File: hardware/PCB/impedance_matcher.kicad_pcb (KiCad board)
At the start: 4 copper layers, 72 x 63 mm, 48 parts, among them Q1 PC817, U1 TLV2372IP

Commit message: Hackerfab Logo
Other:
- board text added: "at CMU"

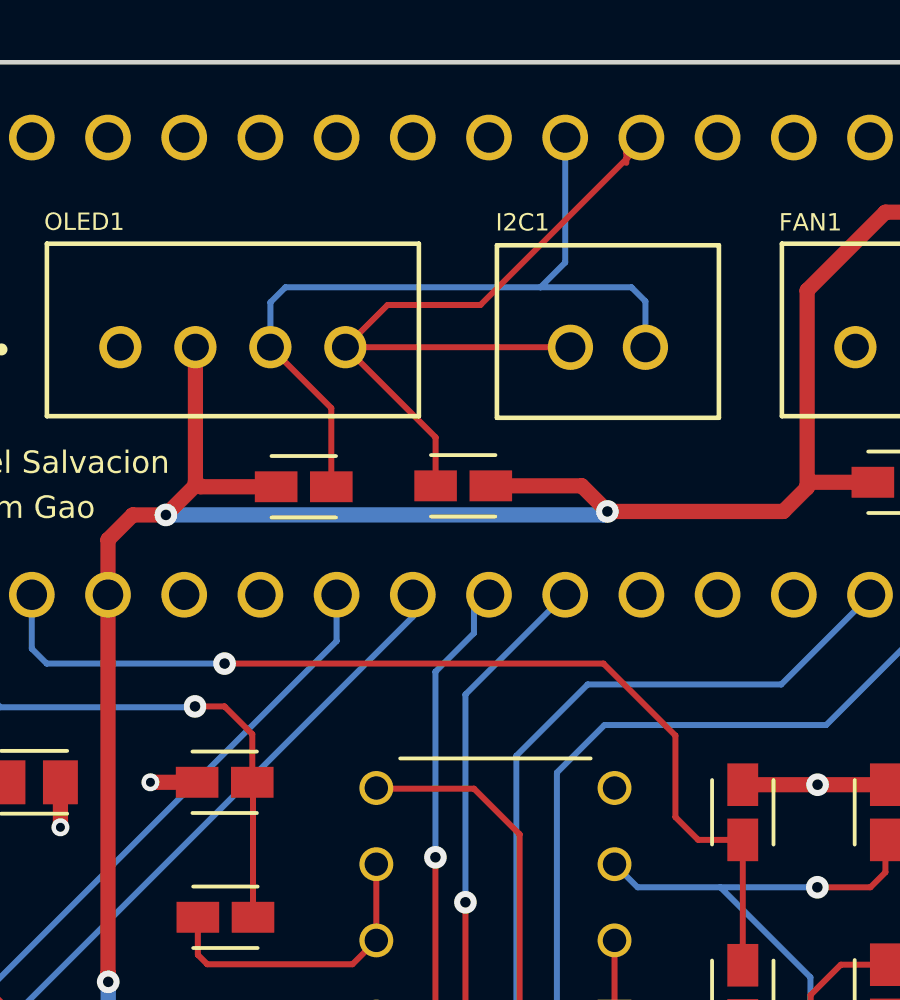
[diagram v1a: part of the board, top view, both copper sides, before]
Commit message: Clean up nets and layers
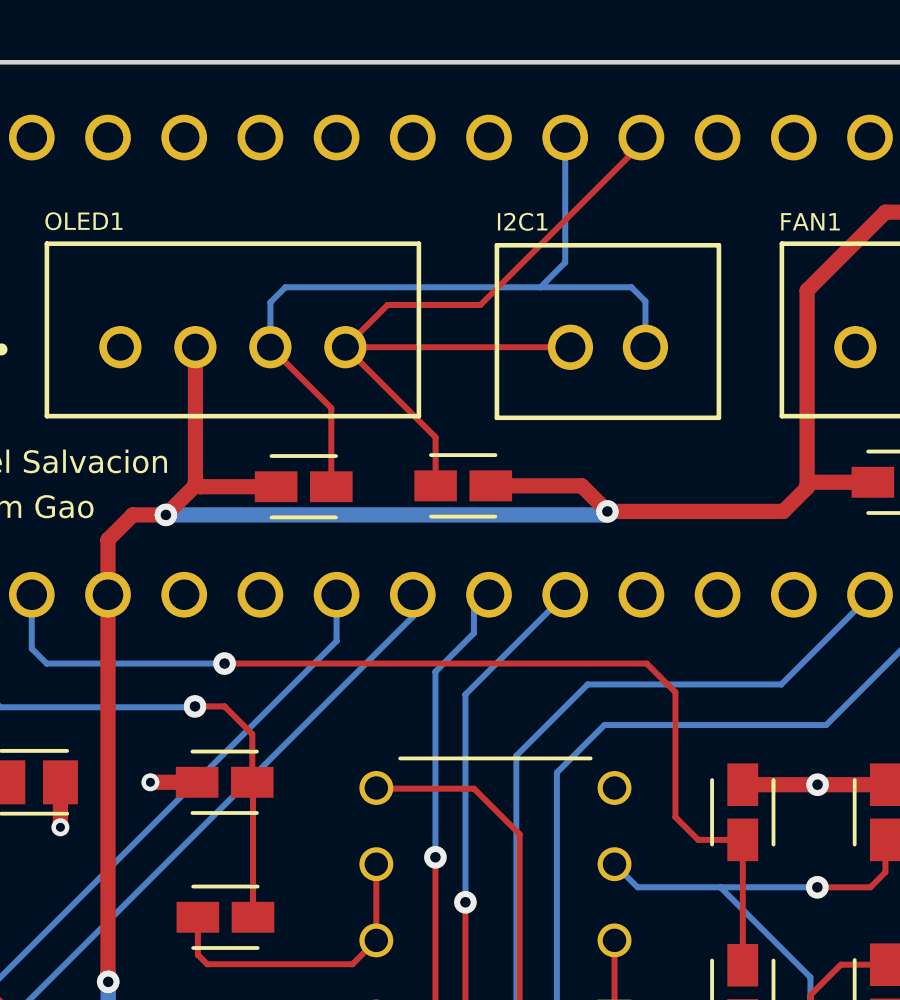
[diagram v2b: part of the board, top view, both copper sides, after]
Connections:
- net Net-(CR1-Pad1) renamed /NET_REVPOL
- net Net-(D1-A) renamed /SW_NODE
- net Net-(DRIVER1-VM) renamed /VM_DRV1
- net Net-(DRIVER2-VM) renamed /VM_DRV2
- net Net-(FAN1-Pin_3) renamed /FAN_CTRL
- net Net-(FB1-Pad2) renamed /FB1_OUT
- net Net-(POWER1-Pin_2) renamed /VIN
- net Net-(STEP_UP0-FB) renamed /FB_DIV
- net Net-(TRANSMIT1-Pin_1) renamed /TX_DRAIN
- net Net-(TRANSMIT1-Pin_2) renamed /TX_GATE
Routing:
- net /FWD_OUT: track 33.6 -> 34.4 mm

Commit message: SWR input protection
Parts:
- added D2: BAV99S, Package_TO_SOT_SMD:SOT-363_SC-70-6, F.Cu at (93.0, 50.5)
- added R14: 1k, Resistor:RESC2012X65, F.Cu at (94.5, 47.5)
- added R15: 1k, Resistor:RESC2012X65, F.Cu at (94.5, 53.5)
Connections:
- U1 pad 3: /FWD_IN -> /FWD_BUF
- U1 pad 5: /REV_IN -> /REV_BUF
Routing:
- net /REV_BUF: track 0.00 -> 33.2 mm
- net /REV_IN: track 43.6 -> 20.2 mm
- net 12V: track 20.8 -> 41.7 mm, vias 0 -> 3
- net /FWD_BUF: track 0.00 -> 14.0 mm, vias 0 -> 1
- net /FWD_IN: track 31.2 -> 25.3 mm, vias 1 -> 0
- net GND: track 22.3 -> 24.9 mm, vias 11 -> 13

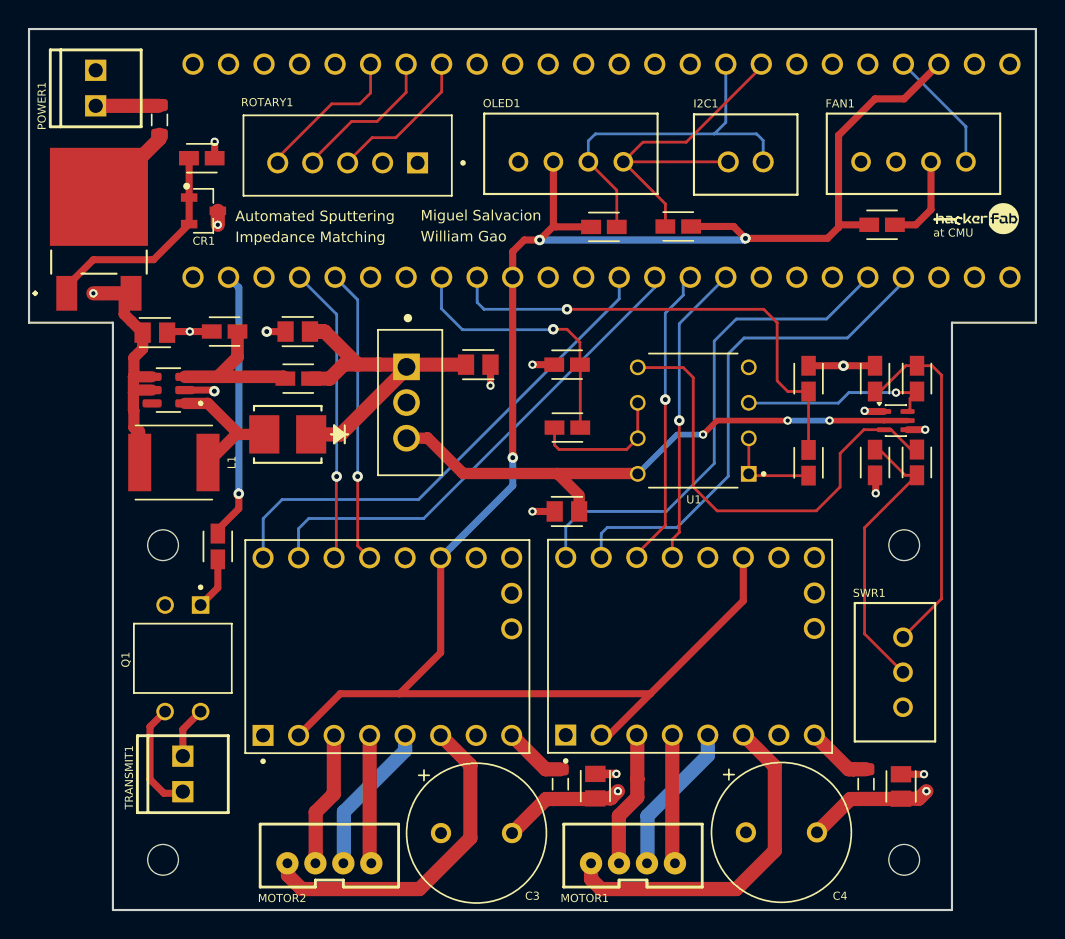
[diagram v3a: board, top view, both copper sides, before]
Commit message: change i2c1, rotary1, oled1, fan1, swr1 to JST PH 2.0mm and update C3/C4 pad1 to be 5V instead of pad2
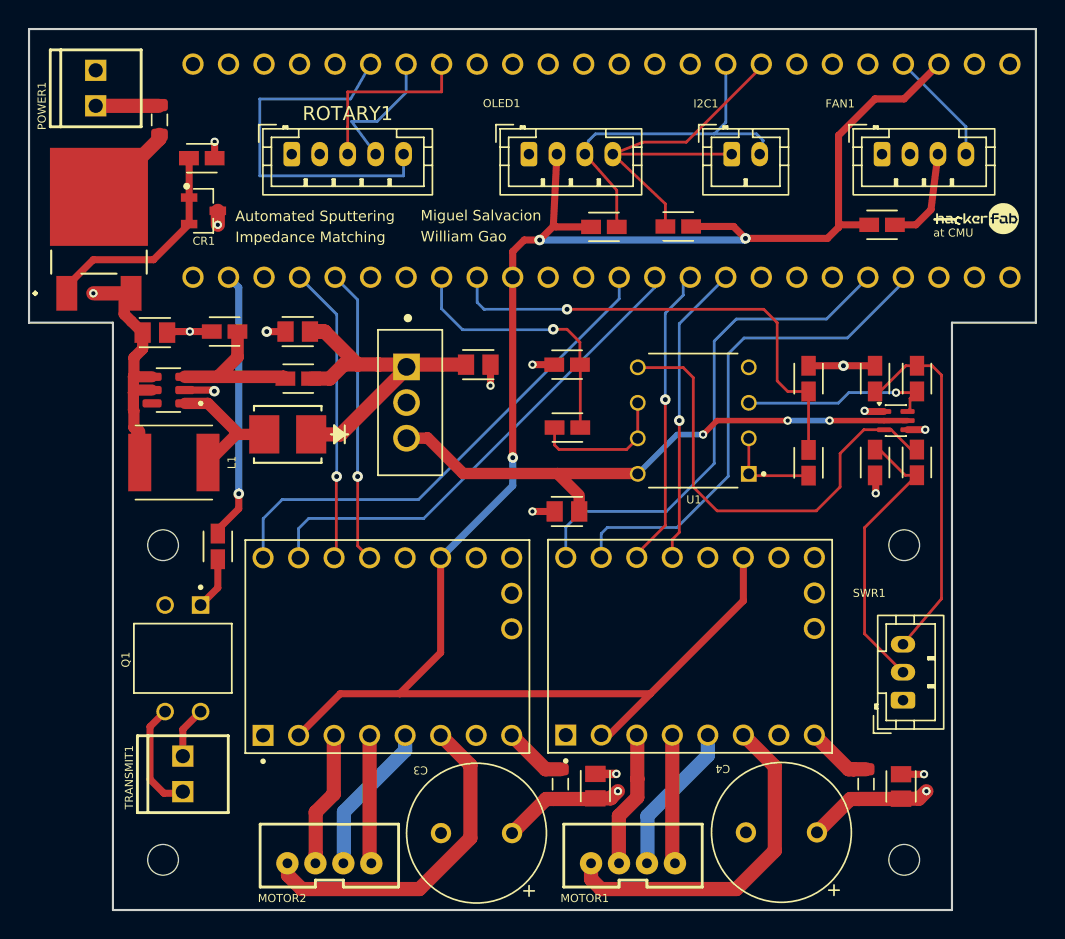
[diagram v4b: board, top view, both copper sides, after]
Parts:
- FAN1, OLED1: footprint Project Connectors:B4B-XH-A -> Connector_JST:JST_PH_B4B-PH-K_1x04_P2.00mm_Vertical
- I2C1: footprint Project Connectors:B2B-XH-A -> Connector_JST:JST_PH_B2B-PH-K_1x02_P2.00mm_Vertical
- ROTARY1: footprint B5B-XH-A:JST_B5B-XH-A -> Connector_JST:JST_PH_B5B-PH-K_1x05_P2.00mm_Vertical
- SWR1: footprint Project Connectors:B3B-XH-A -> Connector_JST:JST_PH_B3B-PH-K_1x03_P2.00mm_Vertical
- moved ROTARY1 4.00 mm to (49.8, 31.4)
- moved I2C1 2.32 mm to (81.2, 31.4), turned to 0 degrees
- moved FAN1 1.60 mm to (92.0, 31.4)
- moved OLED1 0.93 mm to (66.7, 31.4)
- moved SWR1 0.50 mm to (93.5, 70.5)
- turned C3 to 180 degrees
- turned C4 to 180 degrees
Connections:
- C3 pad 1: GND -> 5V
- C3 pad 2: 5V -> GND
- C4 pad 1: GND -> 5V
- C4 pad 2: 5V -> GND
- I2C1 pad 1: /SDA -> /SCL
- I2C1 pad 2: /SCL -> /SDA
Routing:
- net /CLK: track 10.6 -> 26.7 mm
- net /SW: track 10.8 -> 13.2 mm
- net /SCL: track 26.7 -> 29.0 mm
- net /DT: track 10.7 -> 9.68 mm
- net /FAN_CTRL: track 6.45 -> 7.03 mm
- net 3.3V: track 133.8 -> 134.3 mm
- net /FAN: track 8.84 -> 8.29 mm
